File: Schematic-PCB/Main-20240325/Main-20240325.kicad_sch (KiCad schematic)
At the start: 18 parts, among them J1 Conn_01x20_Pin, J2 Conn_01x03_Pin, J3 Conn_01x03_Pin, J4 Conn_01x10_Pin, J5 Conn_02x05_Odd_Even, J6 Conn_01x15_Pin, U1 DEV-16771, U4 MOUDLE-SEEEDUINO-XIAO-ESP32C3

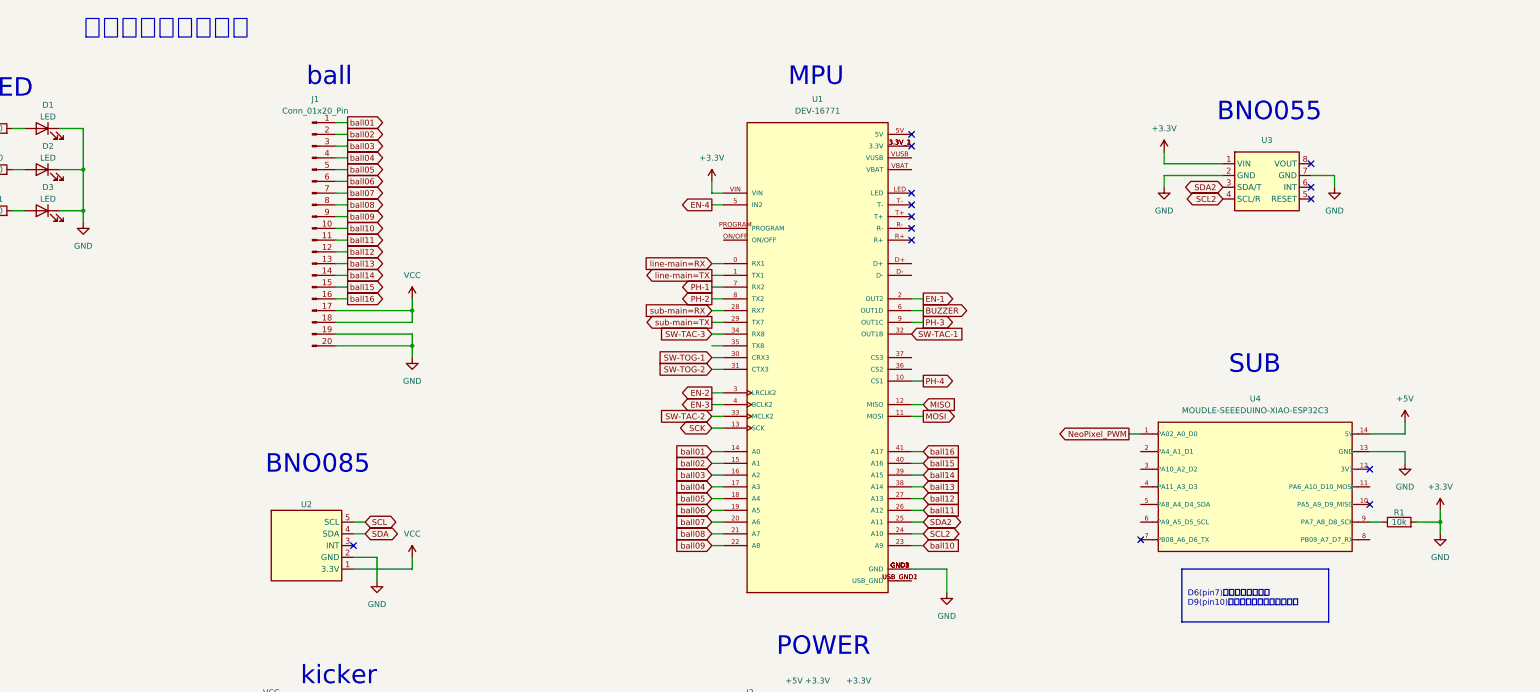
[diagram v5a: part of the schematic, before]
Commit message: ESP32C3周りの修正を手直ししました
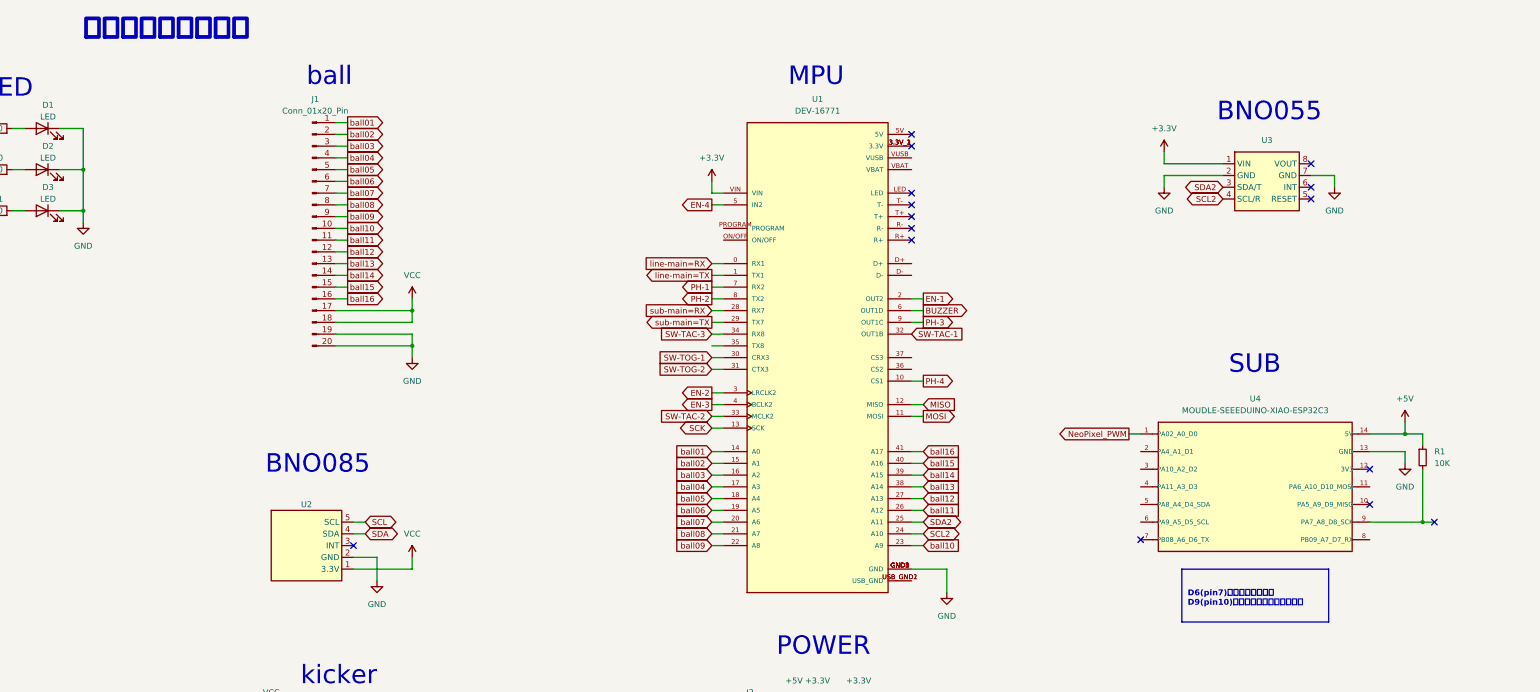
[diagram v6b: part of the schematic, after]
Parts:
- removed R1: 10k, symbol Device:R
- added R1: 10K, symbol Device:R_Small
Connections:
- net +3.3V: no longer C1.2, D1.1 (K), D2.1 (K), D3.1 (K), J1.19 (Pin_19), J1.20 (Pin_20), J2.3 (Pin_3), J3.3 (Pin_3), J4.2 (Pin_2), J5.6 (Pin_6), J6.15 (Pin_15), U1.GND1 (GND), U1.GND2 (GND), U1.GND3 (GND), U1.GND4 (GND), U1.GND5 (GND), U2.2 (GND), U3.2 (GND), U3.7 (GND), U4.13 (GND)
- net +5V: now also R1.1
- net at U4.9 (PA7_A8_D8_SCK): now also R1.2
- new net GND: C1.2, D1.1 (K), D2.1 (K), D3.1 (K), J1.19 (Pin_19), J1.20 (Pin_20), J2.3 (Pin_3), J3.3 (Pin_3), J4.2 (Pin_2), J5.6 (Pin_6), J6.15 (Pin_15), U1.GND1 (GND), U1.GND2 (GND), U1.GND3 (GND), U1.GND4 (GND), U1.GND5 (GND), U2.2 (GND), U3.2 (GND), U3.7 (GND), U4.13 (GND)
- no-connect marks 16 -> 17
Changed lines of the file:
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@@
 	(paper "A3")
 	(junction
-		(at 212.09 119.38)
+		(at -10.16 73.66)
 		(diameter 0)
 		(color 0 0 0 0)
 	)
 	(junction
-		(at -10.16 73.66)
+		(at 208.28 119.38)
 		(diameter 0)
 		(color 0 0 0 0)
@@
 		(color 0 0 0 0)
 	)
+	(junction
+		(at 204.47 100.33)
+		(diameter 0)
+		(color 0 0 0 0)
+	)
+	(no_connect
+		(at 210.82 119.38)
+	)
 	(no_connect
 		(at 97.79 55.88)
@@
 	(wire
 		(pts
-			(xy 212.09 116.84) (xy 212.09 119.38)
+			(xy 208.28 100.33) (xy 208.28 102.87)
 		)
 		(stroke
@@
 	(wire
 		(pts
+			(xy 208.28 107.95) (xy 208.28 119.38)
+		)
+		(stroke
+			(width 0)
+			(type default)
+		)
+	)
+	(wire
+		(pts
 			(xy -81.28 52.07) (xy -81.28 43.18)
 		)
@@
 	(wire
 		(pts
+			(xy 208.28 119.38) (xy 210.82 119.38)
+		)
+		(stroke
+			(width 0)
+			(type default)
+		)
+	)
+	(wire
+		(pts
 			(xy -24.13 163.83) (xy -26.67 163.83)
 		)
@@
 	(wire
 		(pts
-			(xy 207.01 119.38) (xy 212.09 119.38)
-		)
-		(stroke
-			(width 0)
-			(type default)
-		)
-	)
-	(wire
-		(pts
 			(xy -24.13 58.42) (xy -26.67 58.42)
 		)
@@
 	(wire
 		(pts
+			(xy 204.47 100.33) (xy 208.28 100.33)
+		)
+		(stroke
+			(width 0)
+			(type default)
+		)
+	)
+	(wire
+		(pts
 			(xy -81.28 54.61) (xy -81.28 52.07)
 		)
@@
 	(wire
 		(pts
-			(xy 212.09 121.92) (xy 212.09 119.38)
-		)
-		(stroke
-			(width 0)
-			(type default)
-		)
-	)
-	(wire
-		(pts
 			(xy 59.69 215.9) (xy 57.15 215.9)
 		)
@@
 	(wire
 		(pts
-			(xy 199.39 119.38) (xy 196.85 119.38)
+			(xy 196.85 119.38) (xy 208.28 119.38)
 		)
 		(stroke
@@
 		(effects
 			(font
+				(face "游ゴシック")
 				(size 4 4)
+				(bold yes)
 			)
 			(justify left bottom)
@@
 		(effects
 			(font
-				(face "小塚ゴシック Pro R")
+				(face "游ゴシック")
 				(size 1.27 1.27)
+				(bold yes)
 			)
 			(justify left)
@@
 	)
 	(symbol
+		(lib_id "Device:R_Small")
+		(at 208.28 105.41 0)
+		(unit 1)
+		(exclude_from_sim no)
+		(in_bom yes)
+		(on_board yes)
+		(dnp no)
+		(fields_autoplaced yes)
+		(property "Reference" "R1"
+			(at 210.82 104.14 0)
+			(effects
+				(font
+					(size 1.27 1.27)
+				)
+				(justify left)
+			)
+		)
+		(property "Value" "10K"
+			(at 210.82 106.68 0)
+			(effects
+				(font
+					(size 1.27 1.27)
+				)
+				(justify left)
+			)
+		)
+		(property "Footprint" ""
+			(at 208.28 105.41 0)
+			(effects
+				(font
+					(size 1.27 1.27)
+				)
+				(hide yes)
+			)
+		)
+		(property "Datasheet" "~"
+			(at 208.28 105.41 0)
+			(effects
+				(font
+					(size 1.27 1.27)
+				)
+				(hide yes)
+			)
+		)
+		(property "Description" "Resistor, small symbol"
+			(at 208.28 105.41 0)
+			(effects
+				(font
+					(size 1.27 1.27)
+				)
+				(hide yes)
+			)
+		)
+		(pin "2"
+		)
+		(pin "1"
+		)
+		(instances
+			(project "Main-20240325"
+				(path "/d42c2da0-c5d1-4e9e-abe5-6ac5f9ded35c"
+					(reference "R1")
+					(unit 1)
+				)
+			)
+		)
+	)
+	(symbol
 		(lib_id "Device:LED")
 		(at -90.17 52.07 0)
@@
 	)
 	(symbol
-		(lib_id "power:+3.3V")
-		(at 212.09 116.84 0)
-		(unit 1)
-		(exclude_from_sim no)
-		(in_bom yes)
-		(on_board yes)
-		(dnp no)
-		(fields_autoplaced yes)
-		(property "Reference" "#PWR011"
-			(at 212.09 120.65 0)
-			(effects
-				(font
-					(size 1.27 1.27)
-				)
-				(hide yes)
-			)
-		)
-		(property "Value" "+3.3V"
-			(at 212.09 111.76 0)
-			(effects
-				(font
-					(size 1.27 1.27)
-				)
-			)
-		)
-		(property "Footprint" ""
-			(at 212.09 116.84 0)
-			(effects
-				(font
-					(size 1.27 1.27)
-				)
-				(hide yes)
-			)
-		)
-		(property "Datasheet" ""
-			(at 212.09 116.84 0)
-			(effects
-				(font
-					(size 1.27 1.27)
-				)
-				(hide yes)
-			)
-		)
-		(property "Description" "Power symbol creates a global label with name \"+3.3V\""
-			(at 212.09 116.84 0)
-			(effects
-				(font
-					(size 1.27 1.27)
-				)
-				(hide yes)
-			)
-		)
-		(pin "1"
-		)
-		(instances
-			(project "Main-20240325"
-				(path "/d42c2da0-c5d1-4e9e-abe5-6ac5f9ded35c"
-					(reference "#PWR011")
-					(unit 1)
-				)
-			)
-		)
-	)
-	(symbol
 		(lib_name "GND_1")
 		(lib_id "power:GND")
@@
 	)
 	(symbol
-		(lib_id "power:GND")
-		(at 212.09 121.92 0)
-		(unit 1)
-		(exclude_from_sim no)
-		(in_bom yes)
-		(on_board yes)
-		(dnp no)
-		(fields_autoplaced yes)
-		(property "Reference" "#PWR027"
-			(at 212.09 128.27 0)
-			(effects
-				(font
-					(size 1.27 1.27)
-				)
-				(hide yes)
-			)
-		)
-		(property "Value" "GND"
-			(at 212.09 127 0)
-			(effects
-				(font
-					(size 1.27 1.27)
-				)
-			)
-		)
-		(property "Footprint" ""
-			(at 212.09 121.92 0)
-			(effects
-				(font
-					(size 1.27 1.27)
-				)
-				(hide yes)
-			)
-		)
-		(property "Datasheet" ""
-			(at 212.09 121.92 0)
-			(effects
-				(font
-					(size 1.27 1.27)
-				)
-				(hide yes)
-			)
-		)
-		(property "Description" ""
-			(at 212.09 121.92 0)
-			(effects
-				(font
-					(size 1.27 1.27)
-				)
-				(hide yes)
-			)
-		)
-		(pin "1"
-		)
-		(instances
-			(project "Main-20240325"
-				(path "/d42c2da0-c5d1-4e9e-abe5-6ac5f9ded35c"
-					(reference "#PWR027")
-					(unit 1)
-				)
-			)
-		)
-	)
-	(symbol
 		(lib_id "Device:LED")
 		(at -90.17 43.18 0)
@@
 					(unit 1)
 				)
-			)
-		)
-	)
-	(symbol
-		(lib_id "Device:R")
-		(at 203.2 119.38 90)
-		(unit 1)
-		(exclude_from_sim no)
-		(in_bom yes)
-		(on_board yes)
-		(dnp no)
-		(property "Reference" "R1"
-			(at 203.2 117.348 90)
-			(effects
-				(font
-					(size 1.27 1.27)
-				)
-			)
-		)
-		(property "Value" "10k"
-			(at 203.2 119.38 90)
-			(effects
-				(font
-					(size 1.27 1.27)
-				)
-			)
-		)
-		(property "Footprint" ""
-			(at 203.2 121.158 90)
-			(effects
-				(font
-					(size 1.27 1.27)
-				)
-				(hide yes)
-			)
-		)
-		(property "Datasheet" "~"
-			(at 203.2 119.38 0)
-			(effects
-				(font
-					(size 1.27 1.27)
-				)
-				(hide yes)
-			)
-		)
-		(property "Description" "Resistor"
-			(at 203.2 119.38 0)
-			(effects
-				(font
-					(size 1.27 1.27)
-				)
-				(hide yes)
-			)
-		)
-		(pin "2"
-		)
-		(pin "1"
-		)
-		(instances
-			(project "Main-20240325"
-				(path "/d42c2da0-c5d1-4e9e-abe5-6ac5f9ded35c"
-					(reference "R1")
-					(unit 1)
-				)

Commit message: メイン基板の回路図を修正しました
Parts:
- added C2: C, symbol Device:C
- added J7: Conn_02x05_Odd_Even, symbol Connector_Generic:Conn_02x05_Odd_Even
- added JP1, JP11, JP13, JP15, JP3, JP5, JP7, JP9: Jumper_2_Small_Bridged, symbol Jumper:Jumper_2_Small_Bridged
- added JP10, JP12, JP14, JP16, JP2, JP4, JP6, JP8: Jumper_2_Small_Open, symbol Jumper:Jumper_2_Small_Open
- renumbered J3 to J2, J4 to J3, J2 to J4, J6 to J5, J5 to J6, R9 to R1, R10 to R2, R11 to R3, R1 to R4, U2 to U1, U1 to U2, U4 to U3, U3 to U4
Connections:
- net SCL2 is gone; now on net SCL: U2.24 (A10), U4.4 (SCL/R)
- net SDA2 is gone; now on net SDA: U2.25 (A11), U4.3 (SDA/T)
- net +3.3V: now also C2.1; no longer C1.1, U2.VIN
- net +5V: now also C1.1, U2.VIN, J7.2 (Pin_2)
- net GND: now also U2.USB_GND1 (USB_GND), U2.USB_GND2 (USB_GND), C2.2, J7.6 (Pin_6)
- net MISO: now also JP13.1 (A), JP9.1 (A)
- net MOSI: now also JP11.1 (A), JP15.1 (A)
- net PH-1: no longer U2.7 (RX2)
- net PH-2: no longer U2.8 (TX2)
- net PH-4: no longer U2.10 (CS1)
- net SCK: now also JP1.1 (A), JP5.1 (A)
- net SCL: now also JP2.1 (A), JP6.1 (A)
- net SDA: now also JP4.1 (A), JP8.1 (A)
- net Cam2_SS: now reaches U2.36 (CS2)
- net Cam2_SS: now also JP7.1 (A)
- net Cam1_MISO_RX: now reaches J6.1 (Pin_1)
- net Cam1_MISO_RX: now also JP10.2 (B), JP9.2 (B)
- net at J6.3 (Pin_3): now also JP1.2 (B)
- net Cam1_MOSI_TX: now reaches J6.4 (Pin_4)
- net Cam1_MOSI_TX: now also JP11.2 (B), JP12.2 (B)
- net at J6.5 (Pin_5): now also JP2.2 (B)
- net at J6.7 (Pin_7): now also JP3.2 (B)
- net at J6.9 (Pin_9): now also JP4.2 (B)
- new net: J7.5 (Pin_5), JP6.2 (B)
- new net: J7.3 (Pin_3), JP5.2 (B)
- new net: J7.7 (Pin_7), JP7.2 (B)
- new net: J7.9 (Pin_9), JP8.2 (B)
- new net Cam1_SS: JP3.1 (A), U2.10 (CS1)
- new net Cam2_MISO_RX: J7.1 (Pin_1), JP13.2 (B), JP14.2 (B)
- new net Cam2_MOSI_TX: J7.4 (Pin_4), JP15.2 (B), JP16.2 (B)
- new net cam1-main=RX: JP12.1 (A), U2.7 (RX2)
- new net cam1-main=TX: JP10.1 (A), U2.8 (TX2)
- new net cam2-main=RX: JP16.1 (A)
- new net cam2-main=TX: JP14.1 (A)
- no-connect marks 17 -> 23
